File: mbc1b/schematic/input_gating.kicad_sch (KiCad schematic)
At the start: 13 parts

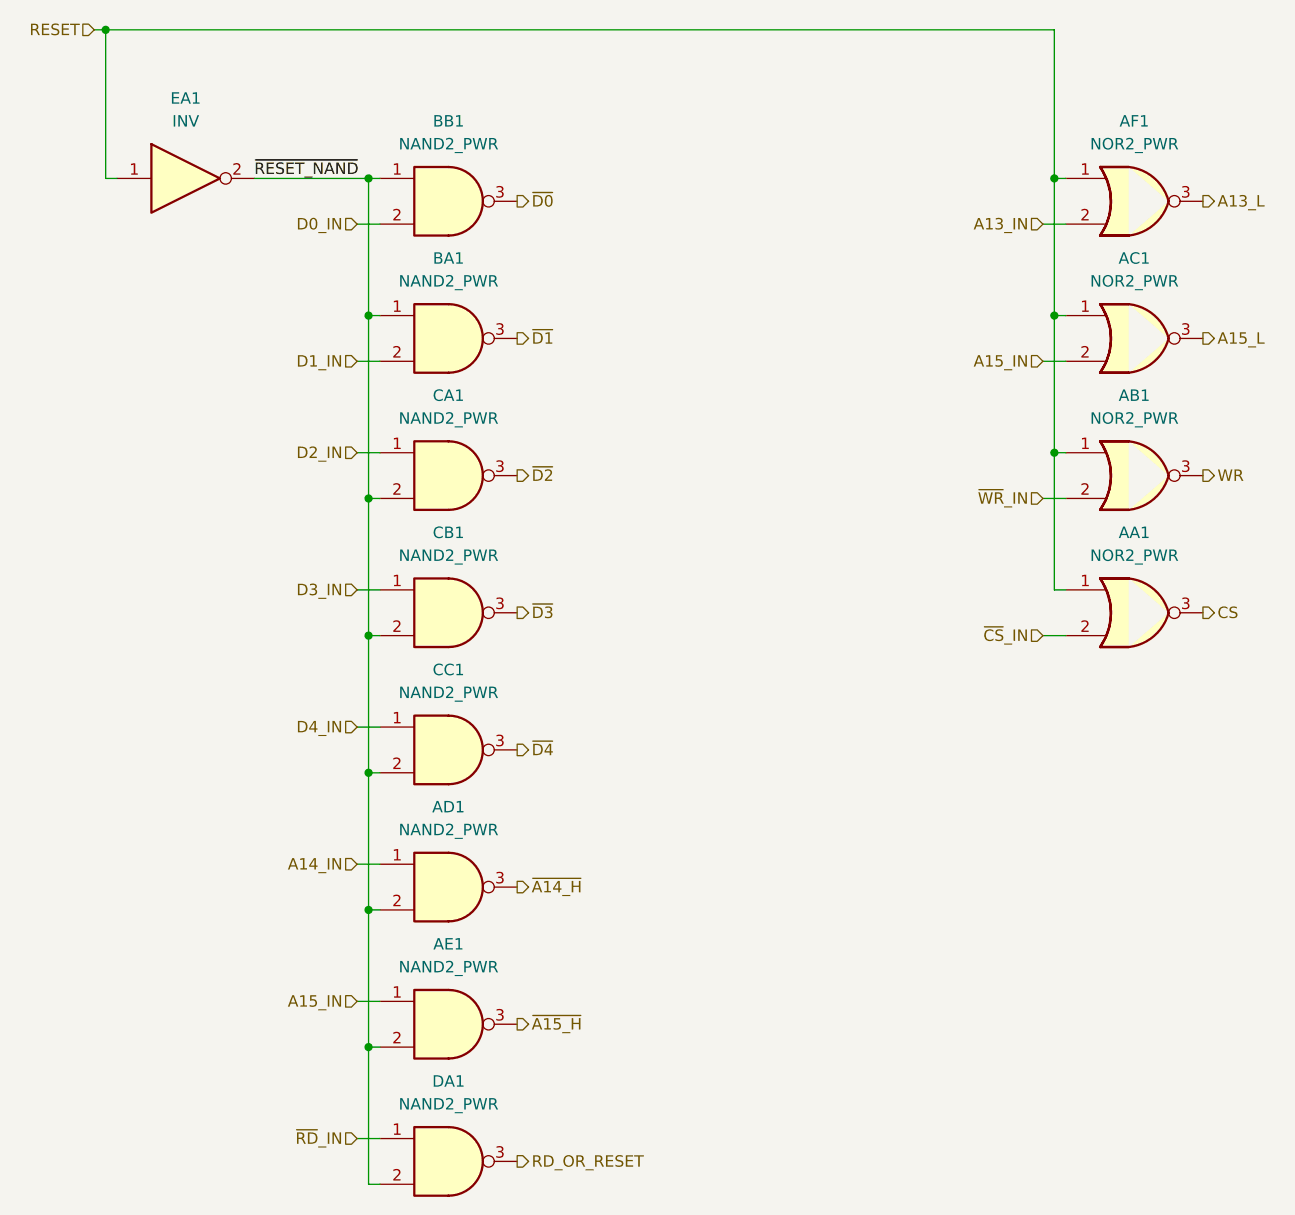
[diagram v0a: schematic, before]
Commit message: Update MBC1B schematic with latest kingfish compatibility
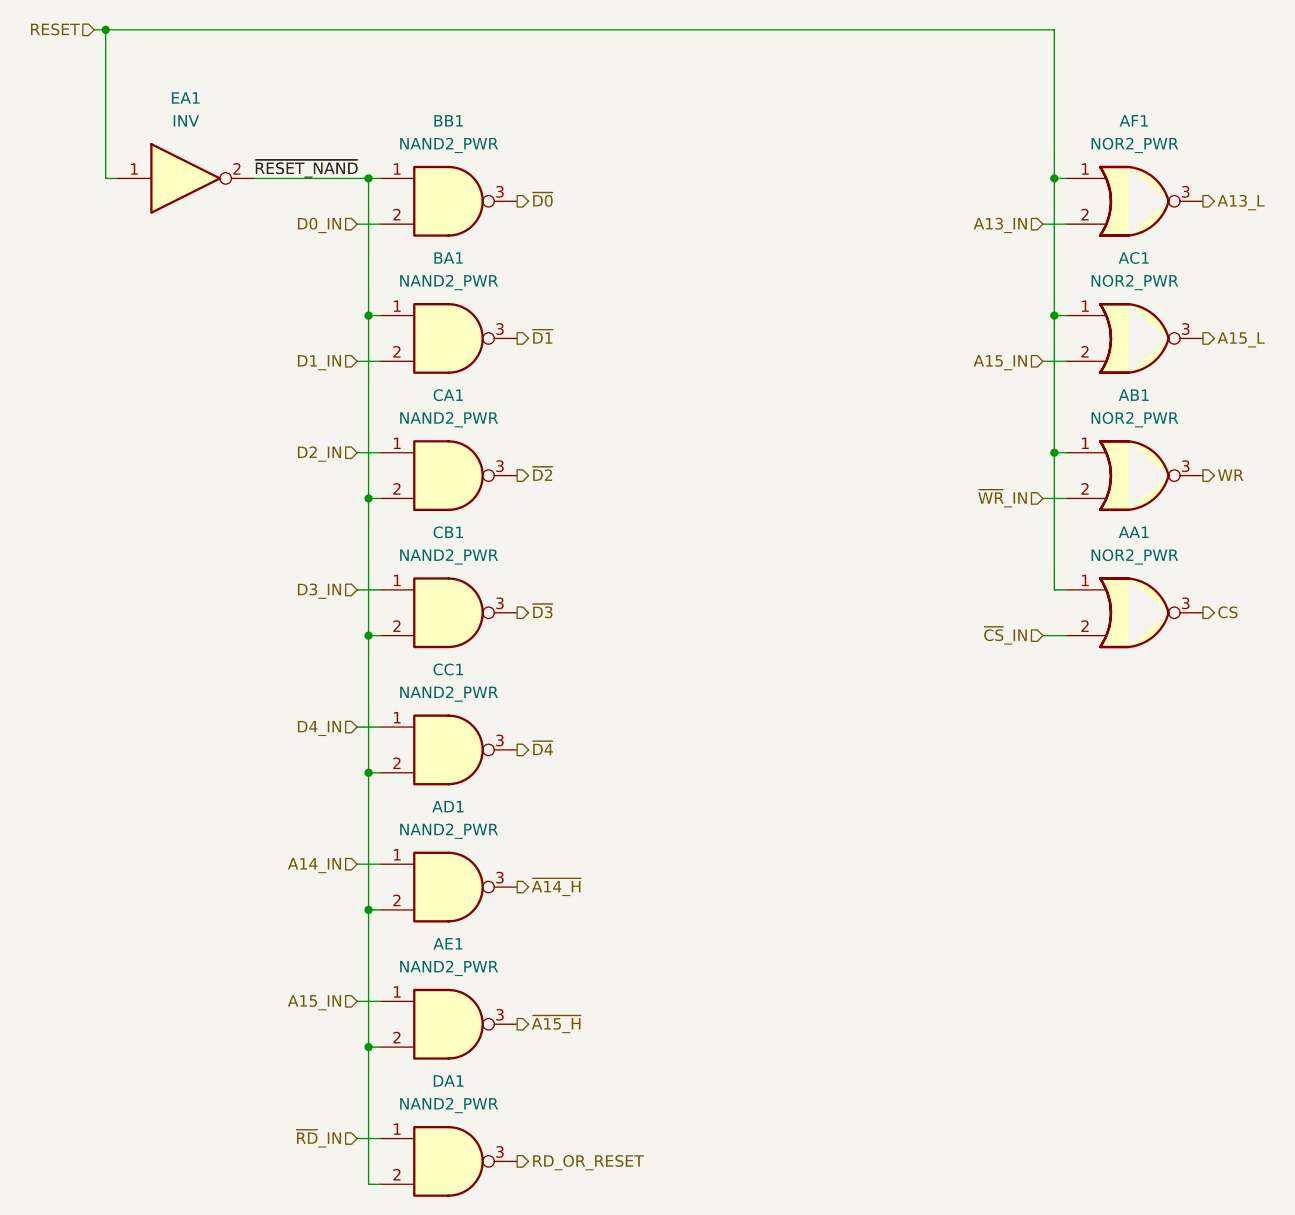
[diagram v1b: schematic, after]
